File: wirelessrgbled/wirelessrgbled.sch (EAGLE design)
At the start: 34 parts, among them J1 1X2-3.5MM, J2 1X2-3.5MM

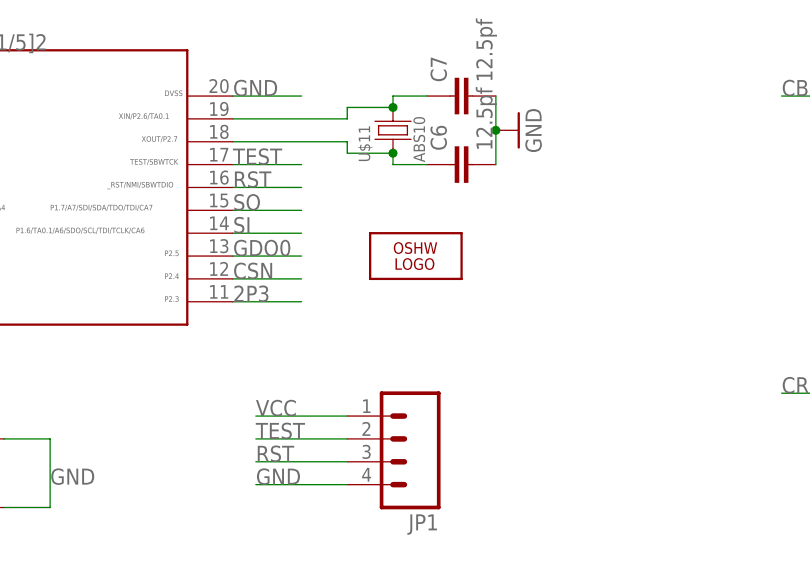
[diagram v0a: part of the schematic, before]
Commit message: Updating wirelessrgbled to v1.1
Adding msp430-cc2500 v1.1
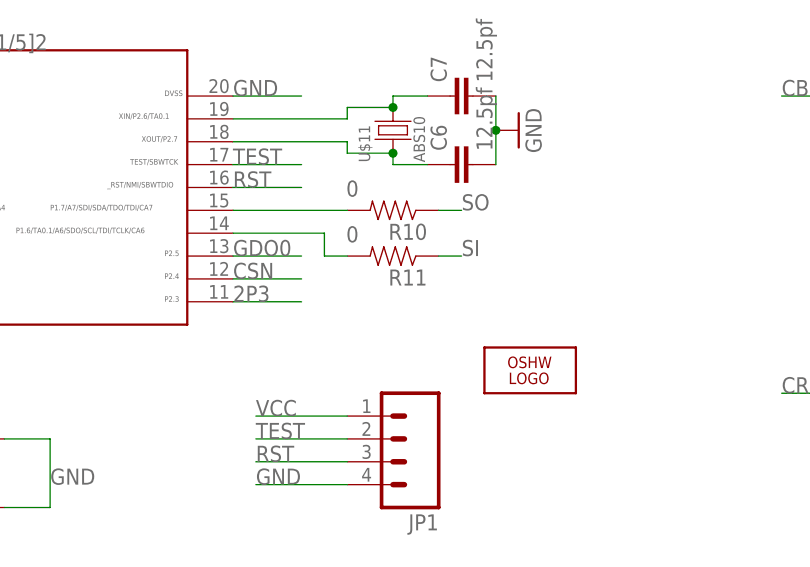
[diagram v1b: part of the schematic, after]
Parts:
- added R10, R11: 0, SparkFun:RESISTOR0805-RES
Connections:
- new net N$7: R10.2, U$2.15
- new net N$9: R11.2, U$2.14
- net SI: now also R11.1; no longer U$2.14
- net SO: now also R10.1; no longer U$2.15
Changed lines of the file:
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@@
 <part name="JP2" library="SparkFun" deviceset="M04" device="PTH"/>
 <part name="LOGO1" library="ohw-logo" deviceset="OSHW_LOGO_10MIL" device="X0200-NT"/>
+<part name="R10" library="SparkFun" deviceset="RESISTOR" device="0805-RES" value="0"/>
+<part name="R11" library="SparkFun" deviceset="RESISTOR" device="0805-RES" value="0"/>
 </parts>
 <sheets>
@@
 <instance part="U$3" gate="G$1" x="-33.02" y="7.62"/>
 <instance part="JP2" gate="G$1" x="-151.13" y="68.58" rot="MR180"/>
-<instance part="LOGO1" gate="G$1" x="-45.72" y="60.96"/>
+<instance part="LOGO1" gate="G$1" x="-33.02" y="48.26"/>
+<instance part="R10" gate="G$1" x="-48.26" y="66.04" smashed="yes" rot="R180">
+<attribute name="NAME" x="-44.45" y="64.5414" size="1.778" layer="95" rot="R180"/>
+<attribute name="VALUE" x="-52.07" y="69.342" size="1.778" layer="96" rot="R180"/>
+</instance>
+<instance part="R11" gate="G$1" x="-48.26" y="60.96" smashed="yes" rot="R180">
+<attribute name="NAME" x="-44.45" y="59.4614" size="1.778" layer="95" rot="R180"/>
+<attribute name="VALUE" x="-52.07" y="64.262" size="1.778" layer="96" rot="R180"/>
+</instance>
 </instances>
 <busses>
@@
 </segment>
 <segment>
-<pinref part="U$2" gate="G$1" pin="14"/>
-<label x="-66.04" y="63.5" size="1.778" layer="95"/>
-<wire x1="-58.42" y1="63.5" x2="-66.04" y2="63.5" width="0.1524" layer="91"/>
+<pinref part="R11" gate="G$1" pin="1"/>
+<wire x1="-43.18" y1="60.96" x2="-40.64" y2="60.96" width="0.1524" layer="91"/>
+<label x="-40.64" y="60.96" size="1.778" layer="95"/>
 </segment>
 </net>
@@
 </segment>
 <segment>
-<pinref part="U$2" gate="G$1" pin="15"/>
-<label x="-66.04" y="66.04" size="1.778" layer="95"/>
-<wire x1="-66.04" y1="66.04" x2="-58.42" y2="66.04" width="0.1524" layer="91"/>
+<pinref part="R10" gate="G$1" pin="1"/>
+<wire x1="-43.18" y1="66.04" x2="-40.64" y2="66.04" width="0.1524" layer="91"/>
+<label x="-40.64" y="66.04" size="1.778" layer="95"/>
 </segment>
 </net>
@@
 </segment>
 </net>
+<net name="N$7" class="0">
+<segment>
+<pinref part="R10" gate="G$1" pin="2"/>
+<pinref part="U$2" gate="G$1" pin="15"/>
+<wire x1="-53.34" y1="66.04" x2="-66.04" y2="66.04" width="0.1524" layer="91"/>
+</segment>
+</net>
+<net name="N$9" class="0">
+<segment>
+<pinref part="R11" gate="G$1" pin="2"/>
+<wire x1="-53.34" y1="60.96" x2="-55.88" y2="60.96" width="0.1524" layer="91"/>
+<wire x1="-55.88" y1="60.96" x2="-55.88" y2="63.5" width="0.1524" layer="91"/>
+<pinref part="U$2" gate="G$1" pin="14"/>
+<wire x1="-55.88" y1="63.5" x2="-66.04" y2="63.5" width="0.1524" layer="91"/>
+</segment>
+</net>
 </nets>
 </sheet>
 </sheets>
+<errors>
+</errors>
 </schematic>
 </drawing>
